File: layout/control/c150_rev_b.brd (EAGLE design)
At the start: 200 x 50 mm, 81 parts, among them IC1 STM32F103C8T, IC2 LP2985-SOT23-5, IC3 IC_USBLC6-2, IC4 IC_USBLC6-2, IC5 LT1619ES8, IC6 LP2985-SOT23-5, IC7 IRF7470, SW1 2P2T, T1 LPISR, Y1 532-CRYSTAL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

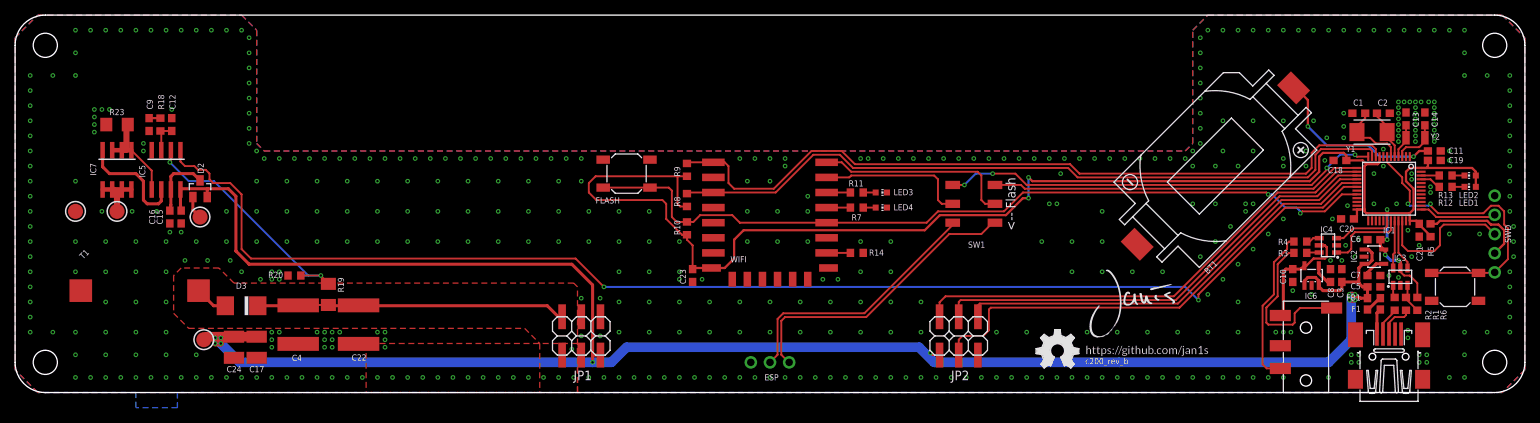
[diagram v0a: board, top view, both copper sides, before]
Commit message: Added new control board versions and TRS adapter
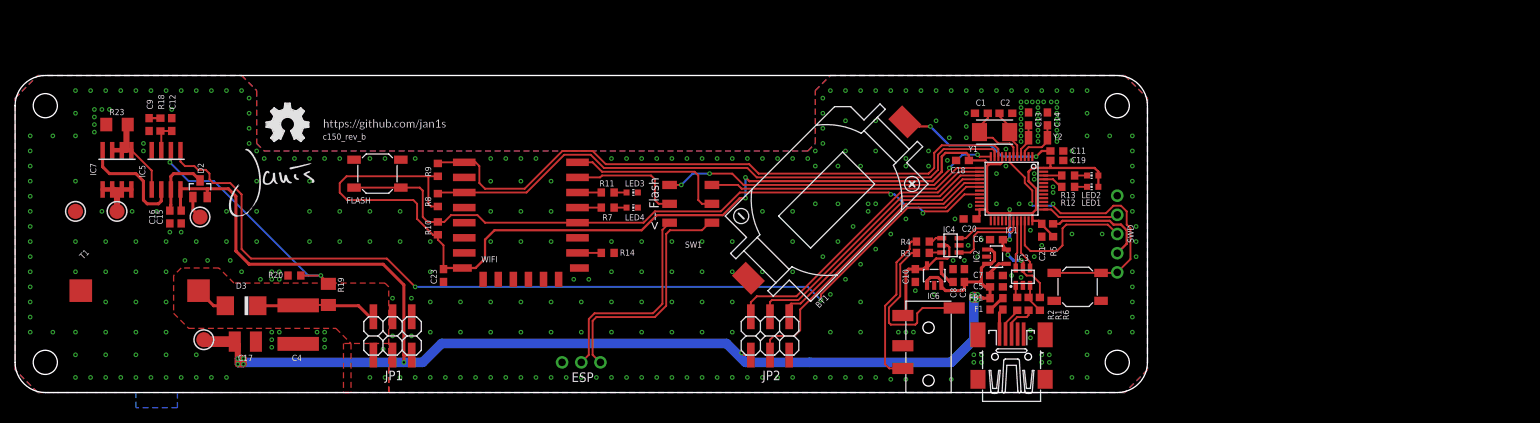
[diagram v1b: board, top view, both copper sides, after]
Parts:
- removed C22: 1µF/250V, rcl:C2220K
- removed C24: 100µF/6.3V, rcl:C1210
- moved U$1 115.1 mm to (28.0, 23.0)
- moved LOGO2 106.3 mm to (33.2, 33.2)
- moved U$5 105.4 mm to (40.8, 35.0)
- moved BT1 51.7 mm to (107.5, 25.5)
- moved C1 50.0 mm to (128.0, 37.0)
- moved C10 50.0 mm to (119.2, 15.5)
- moved C11 50.0 mm to (138.0, 32.0)
- moved C13 50.0 mm to (134.2, 36.2)
- moved C14 50.0 mm to (136.8, 36.2)
- moved C18 50.0 mm to (125.5, 30.8)
- moved C19 50.0 mm to (138.0, 30.8)
- moved C2 50.0 mm to (131.2, 37.0)
- moved C20 50.0 mm to (126.5, 23.0)
- moved C21 50.0 mm to (136.0, 21.5)
- moved C3 50.0 mm to (125.8, 15.5)
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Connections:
- net +5V: no longer C24.1
- net GND: no longer C22.2, C24.2
- net HV: no longer C22.1
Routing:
- net +5V: track 300.7 -> 205.3 mm
- net HV_EN: track 176.3 -> 126.3 mm
- net SPI1_SCK: track 61.6 -> 36.6 mm
- net SPI1_MOSI: track 65.0 -> 40.0 mm
- net HV: track 42.9 -> 17.9 mm
- net NX_RCK: track 58.7 -> 33.7 mm
- net NX_EN: track 64.4 -> 39.4 mm
- net RFMOD_RST: track 101.3 -> 84.3 mm
- net RFMOD_EN: track 97.7 -> 80.7 mm
- net +3V3: track 199.5 -> 182.5 mm
- net RFMOD_FLASH: track 108.5 -> 91.5 mm
- net USART2_TX: track 58.2 -> 45.7 mm
- net USART2_RX: track 49.3 -> 36.8 mm
- net N$31: track 39.6 -> 32.7 mm
- net N$32: track 34.8 -> 27.9 mm
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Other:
- board size 200 x 50 mm -> 150 x 42 mm
- board text added: "c150_rev_b"
- board text removed: "c200_rev_b"
